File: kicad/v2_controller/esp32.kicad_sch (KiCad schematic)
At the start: 21 parts, among them J3 Conn_02x10_Odd_Even, J4 Conn_02x10_Odd_Even, J5 Conn_02x04_Odd_Even, J6 Conn_02x03_Odd_Even, Q1 S8050, Q2 S8050, SW18 Boot, SW19 Reset, U3 74AHCT1G125

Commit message: [kicad] more routing
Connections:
- net COL0: now also J3.18 (Pin_18); no longer J3.4 (Pin_4)
- net COL1: now also J3.16 (Pin_16); no longer J3.6 (Pin_6)
- net COL2: now also J3.14 (Pin_14); no longer J3.8 (Pin_8)
- net COL3: now also J3.12 (Pin_12); no longer J3.10 (Pin_10)
- net COL4: now also J3.10 (Pin_10); no longer J3.12 (Pin_12)
- net COL5: now also J3.8 (Pin_8); no longer J3.14 (Pin_14)
- net COL6: now also J3.6 (Pin_6); no longer J3.16 (Pin_16)
- net COL7: now also J3.4 (Pin_4); no longer J3.18 (Pin_18)
- net LED_LEFT_DIN: now also J4.17 (Pin_17)
- net LED_RIGHT_DIN: no longer J3.17 (Pin_17)
- net ROW0: now also J3.13 (Pin_13); no longer J3.3 (Pin_3)
- net ROW1: now also J3.11 (Pin_11); no longer J3.5 (Pin_5)
- net ROW2: now also J3.9 (Pin_9); no longer J3.7 (Pin_7)
- net ROW3: now also J3.7 (Pin_7); no longer J3.9 (Pin_9)
- net ROW4: now also J3.5 (Pin_5); no longer J3.11 (Pin_11)
- net ROW5: now also J3.3 (Pin_3); no longer J3.13 (Pin_13)

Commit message: [kicad] update part numbers for headers
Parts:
- J3, J4: LCSC Part # C5157633 -> C3405
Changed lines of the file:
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@@
       (effects (font (size 1.27 1.27)) hide)
     )
-    (property "LCSC Part #" "C5157633" (at 214.63 93.98 0)
+    (property "LCSC Part #" "C3405" (at 214.63 93.98 0)
       (effects (font (size 1.27 1.27)) hide)
     )
@@
       (effects (font (size 1.27 1.27)) hide)
     )
-    (property "LCSC Part #" "C5157633" (at 214.63 49.53 0)
+    (property "LCSC Part #" "C3405" (at 214.63 49.53 0)
       (effects (font (size 1.27 1.27)) hide)
     )

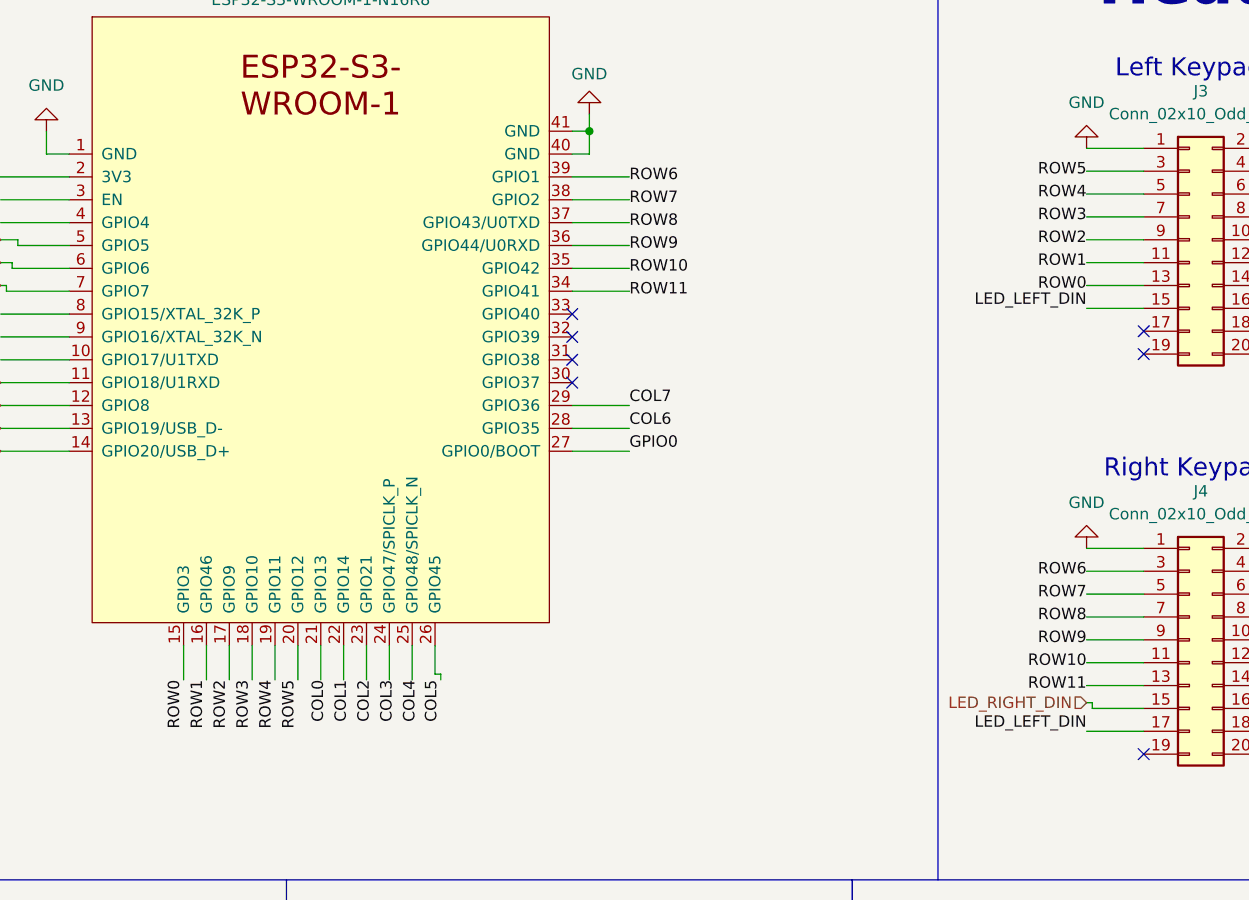
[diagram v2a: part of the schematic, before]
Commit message: [kicad] finish connecting remaining rows
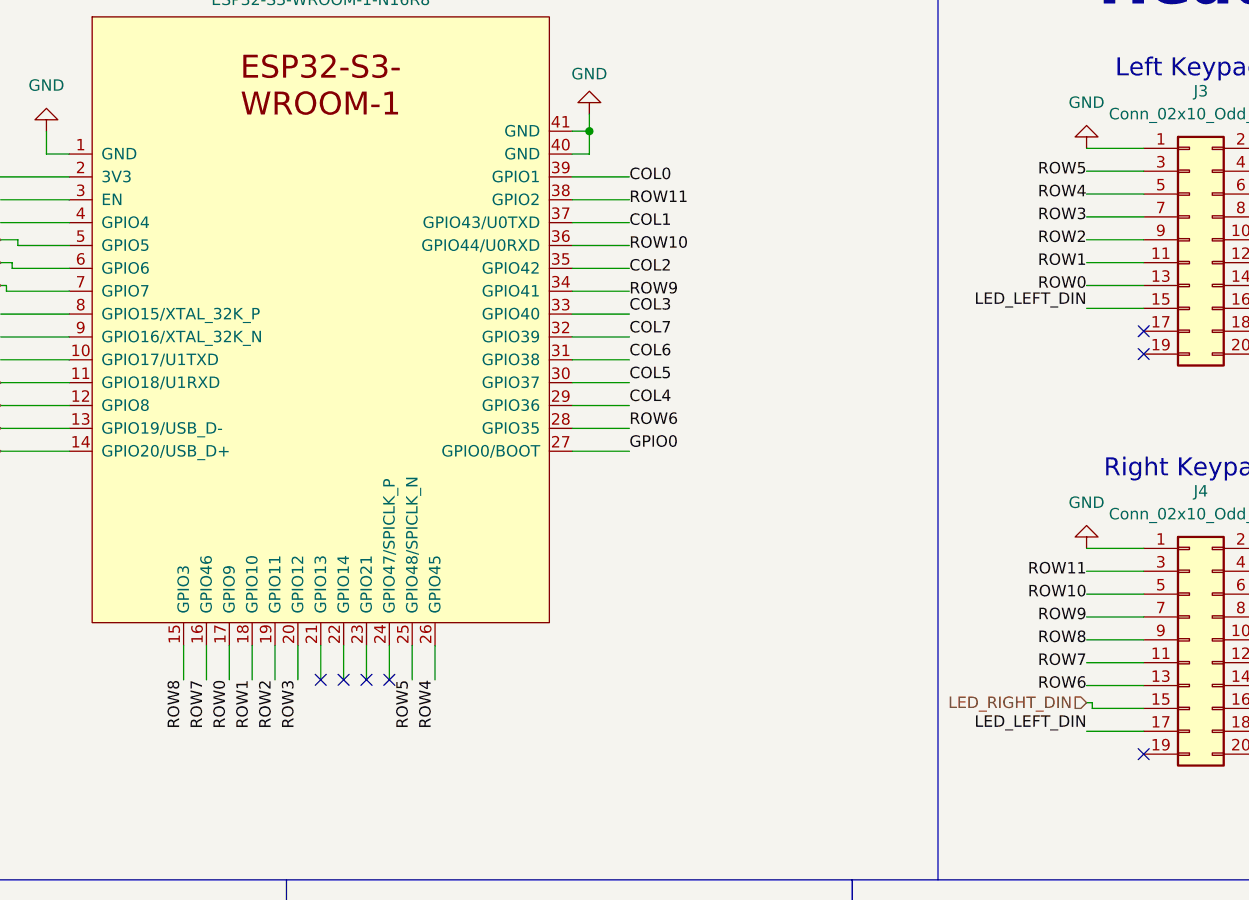
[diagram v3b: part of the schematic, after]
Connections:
- net COL0: now also U?.39 (GPIO1); no longer U?.21 (GPIO13)
- net COL1: now also U?.37 (GPIO43/U0TXD); no longer U?.22 (GPIO14)
- net COL2: now also U?.35 (GPIO42); no longer U?.23 (GPIO21)
- net COL3: now also U?.33 (GPIO40); no longer U?.24 (GPIO47/SPICLK_P)
- net COL4: now also U?.29 (GPIO36); no longer U?.25 (GPIO48/SPICLK_N)
- net COL5: now also U?.30 (GPIO37); no longer U?.26 (GPIO45)
- net COL6: now also U?.31 (GPIO38); no longer U?.28 (GPIO35)
- net COL7: now also U?.32 (GPIO39); no longer U?.29 (GPIO36)
- net ROW0: now also U?.17 (GPIO9); no longer U?.15 (GPIO3)
- net ROW1: now also U?.18 (GPIO10); no longer U?.16 (GPIO46)
- net ROW10: now also J4.5 (Pin_5), U?.36 (GPIO44/U0RXD); no longer J4.11 (Pin_11), U?.35 (GPIO42)
- net ROW11: now also J4.3 (Pin_3), U?.38 (GPIO2); no longer J4.13 (Pin_13), U?.34 (GPIO41)
- net ROW2: now also U?.19 (GPIO11); no longer U?.17 (GPIO9)
- net ROW3: now also U?.20 (GPIO12); no longer U?.18 (GPIO10)
- net ROW4: now also U?.26 (GPIO45); no longer U?.19 (GPIO11)
- net ROW5: now also U?.25 (GPIO48/SPICLK_N); no longer U?.20 (GPIO12)
- net ROW6: now also J4.13 (Pin_13), U?.28 (GPIO35); no longer J4.3 (Pin_3), U?.39 (GPIO1)
- net ROW7: now also J4.11 (Pin_11), U?.16 (GPIO46); no longer J4.5 (Pin_5), U?.38 (GPIO2)
- net ROW8: now also J4.9 (Pin_9), U?.15 (GPIO3); no longer J4.7 (Pin_7), U?.37 (GPIO43/U0TXD)
- net ROW9: now also J4.7 (Pin_7), U?.34 (GPIO41); no longer J4.9 (Pin_9), U?.36 (GPIO44/U0RXD)

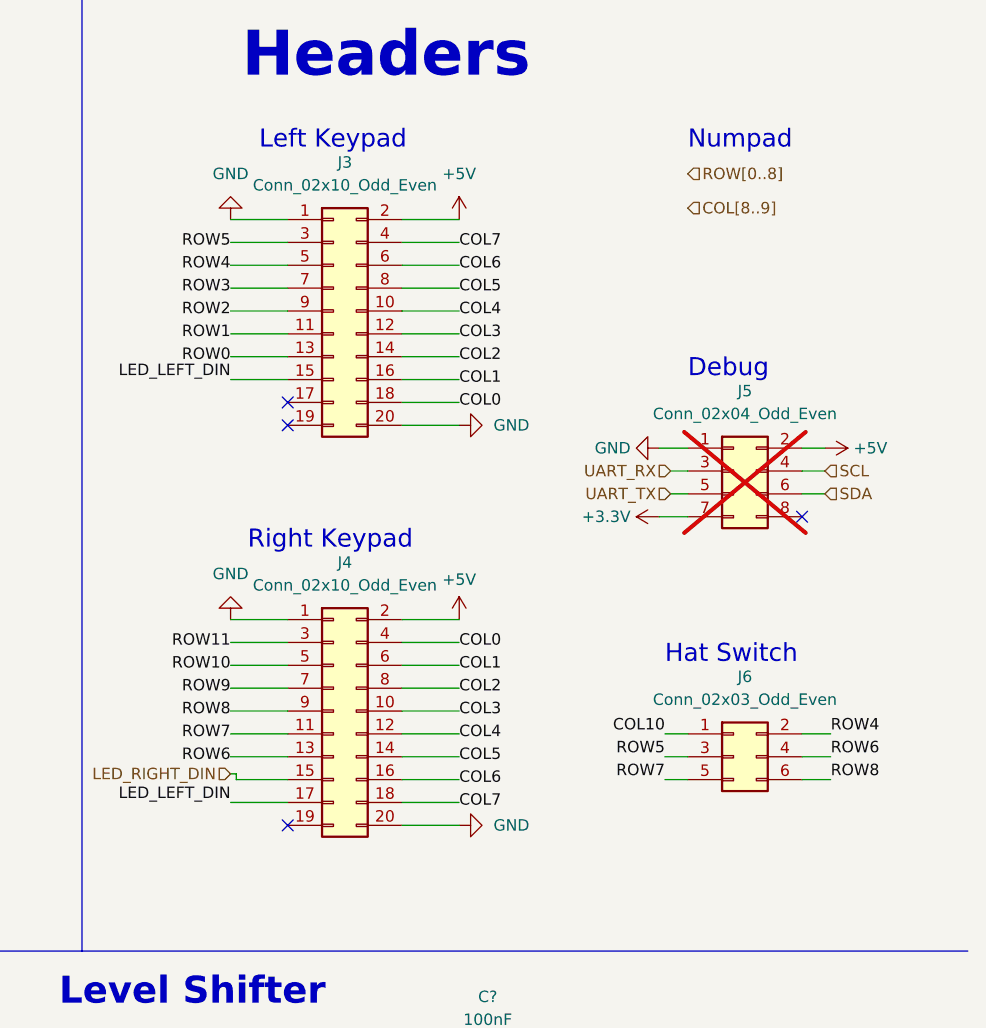
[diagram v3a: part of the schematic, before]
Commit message: [kicad] add a header for an external reset button
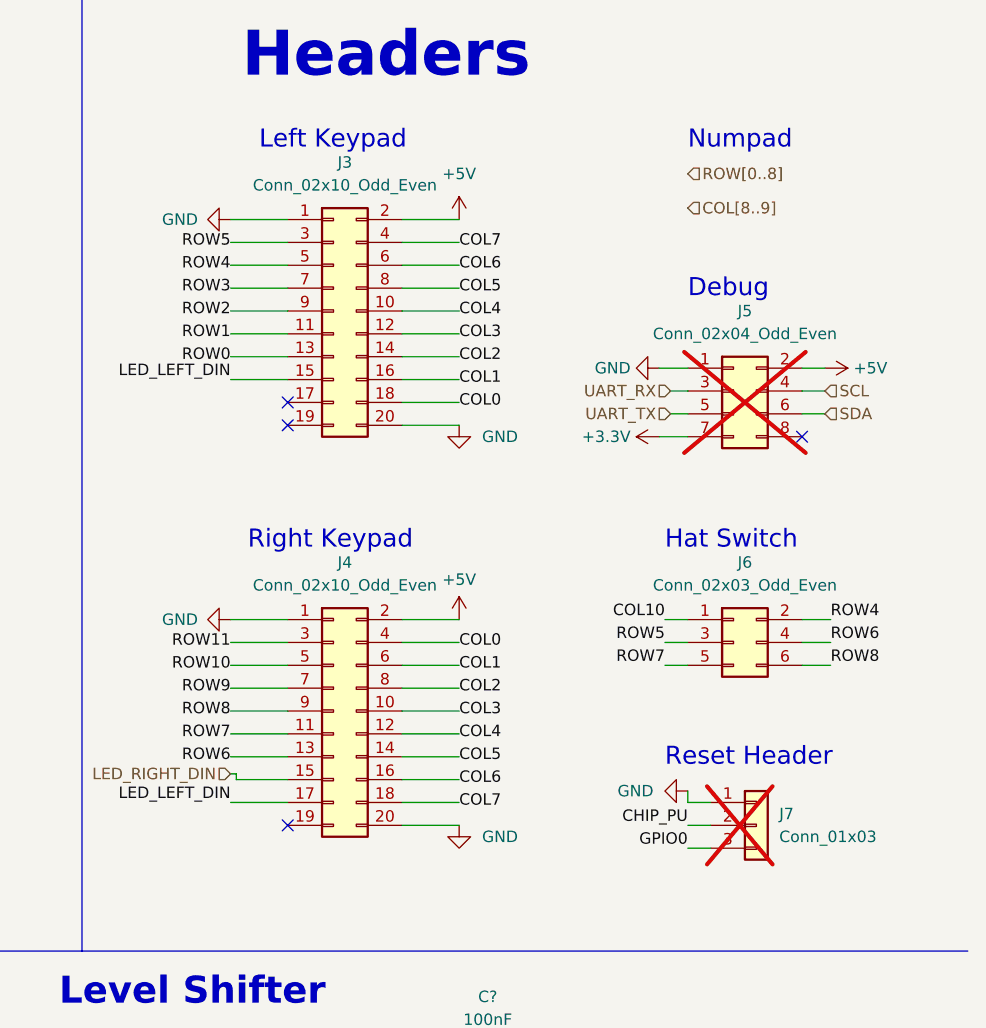
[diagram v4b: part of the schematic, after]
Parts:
- added J7: Conn_01x03, Connector_PinSocket_2.54mm:PinSocket_1x03_P2.54mm_Vertical, symbol Connector_Generic:Conn_01x03
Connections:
- net CHIP_PU: now also J7.2 (Pin_2)
- net GND: now also J7.1 (Pin_1)
- net GPIO0: now also J7.3 (Pin_3)
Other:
- note added: "Reset Header"
- moved on the sheet: J5, J6

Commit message: [kicad] add JLCPCB offset for the ESP32 module
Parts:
- U?: JLCPCB Position Offset (none) -> 0.0,-0.635
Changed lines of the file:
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@@
       (effects (font (size 1.27 1.27)) hide)
     )
-    (property "LCSC Part #" "C2913202" (at 138.43 22.225 0)
+    (property "LCSC Part #" "C2913202" (at 142.24 23.495 0)
       (effects (font (size 1.27 1.27)) hide)
     )
+    (property "JLCPCB Position Offset" "0.0,-0.635" (at 157.48 23.495 0)
+      (effects (font (size 1.27 1.27)) hide)
+    )

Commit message: [kicad] update JLCPCB socket offset to reflect flipped position
I'm using this socket flipped, so I had previously incorrectly
set the X axis up negative from what the value needed to be.
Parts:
- U?: JLCPCB Position Offset 0.0,-0.635 -> 0.0,0.635
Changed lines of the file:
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@@
       (effects (font (size 1.27 1.27)) hide)
     )
-    (property "JLCPCB Position Offset" "0.0,-0.635" (at 157.48 23.495 0)
+    (property "JLCPCB Position Offset" "0.0,0.635" (at 157.48 23.495 0)
       (effects (font (size 1.27 1.27)) hide)
     )
+    (property "Manufacturer Part #" "" (at 90.17 73.025 0)
+      (effects (font (size 1.27 1.27)) hide)
+    )

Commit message: [kicad] fix incorrect JLCPCB part number for R1
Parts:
- R?: LCSC Part # C52923 -> C25744
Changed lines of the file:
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@@
       (effects (font (size 1.27 1.27)) hide)
     )
-    (property "LCSC Part #" "C52923" (at 29.21 95.25 0)
+    (property "LCSC Part #" "C25744" (at 29.21 95.25 0)
       (effects (font (size 1.27 1.27)) hide)
     )
